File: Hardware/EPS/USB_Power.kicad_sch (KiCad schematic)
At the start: 5 parts

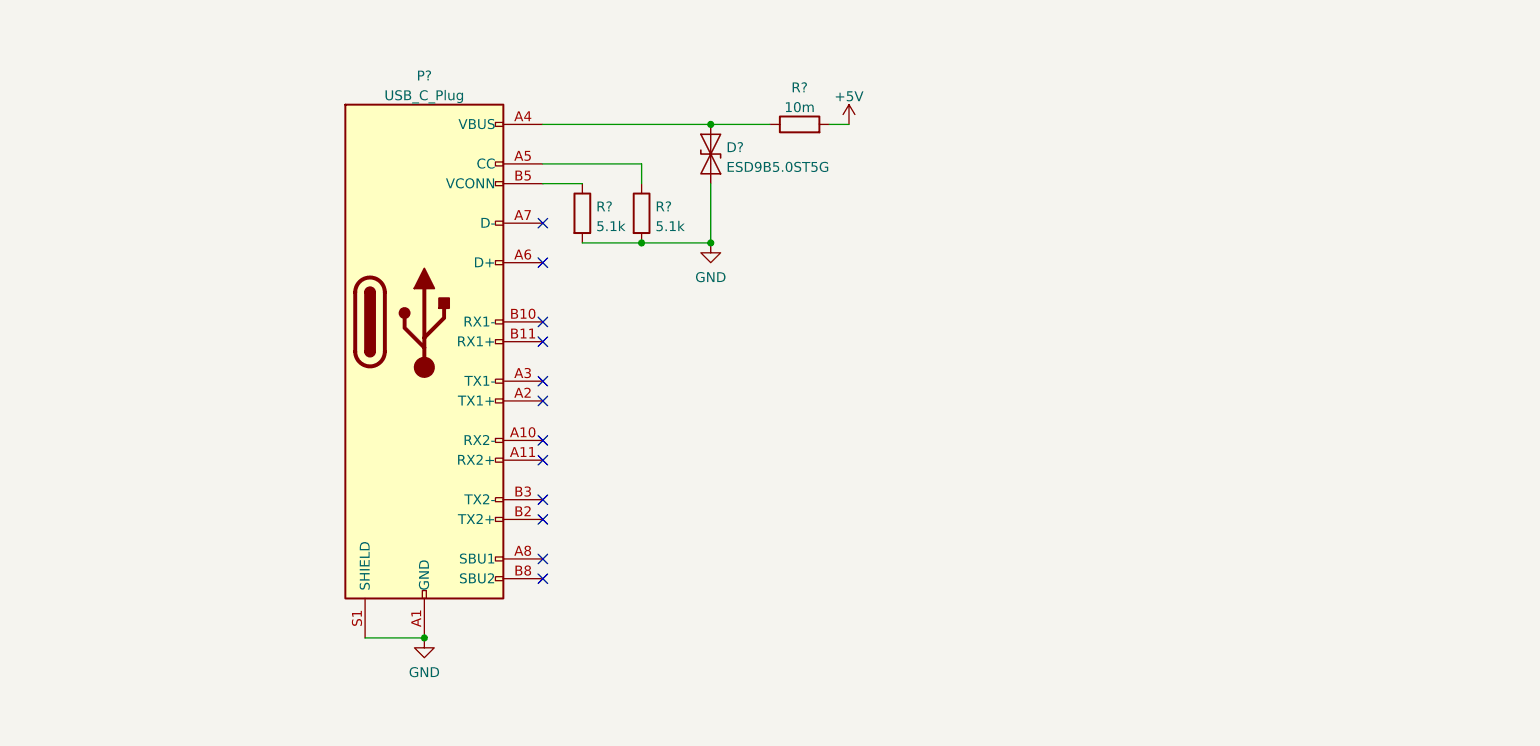
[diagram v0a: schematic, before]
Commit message: Added Power sheet and ESD Protection
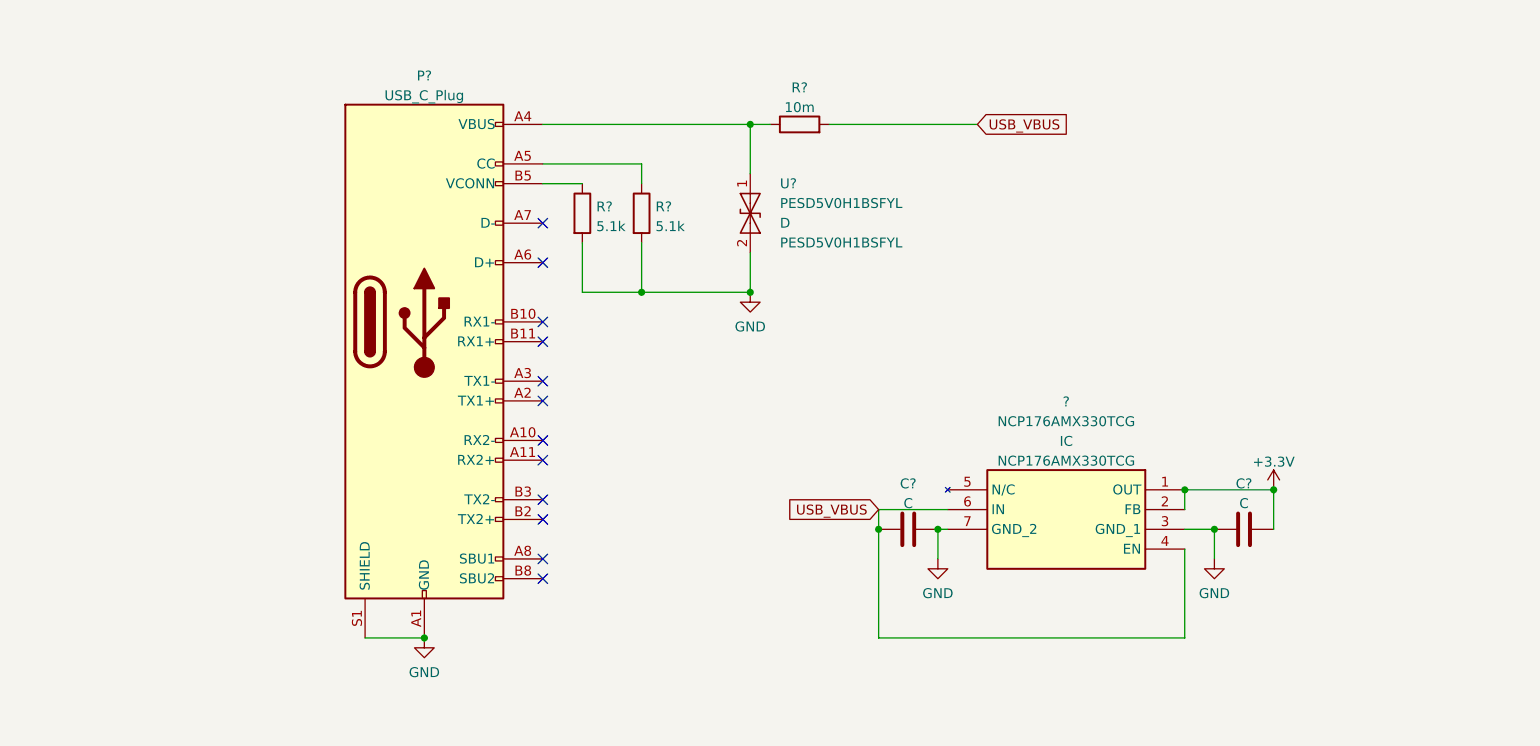
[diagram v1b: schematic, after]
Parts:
- removed D?: ESD9B5.0ST5G, Diode_SMD:D_SOD-923, symbol Diode:ESD9B5.0ST5G
- added ?: NCP176AMX330TCG, symbol NCP176AMX330TCG:NCP176AMX330TCG
- added C? (x2): C, symbol Device:C
- added U?: PESD5V0H1BSFYL, symbol PESD5V0H1BSFYL:PESD5V0H1BSFYL
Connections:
- net GND: now also ?.3 (GND_1), ?.7 (GND_2), C?.1, C?.2, U?.2 (A2)
- net at P?.A4 (VBUS), P?.A9 (VBUS), P?.B4 (VBUS)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: now also U?.1 (A1)
- net +5V renamed USB_VBUS
- net USB_VBUS: now also ?.4 (EN), ?.6 (IN), C?.2
- new net +3.3V: ?.1 (OUT), ?.2 (FB), C?.1

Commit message: EPS v0.0.1
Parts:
- removed R?: 10m, symbol Device:R
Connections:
- net USB_VBUS: now also P?.A4 (VBUS), P?.A9 (VBUS), P?.B4 (VBUS), P?.B9 (VBUS), U?.1 (A1)
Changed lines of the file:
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@@
     (stroke (width 0) (type default) (color 0 0 0 0))
   )
-  (wire (pts (xy 158.75 60.96) (xy 177.8 60.96))
-    (stroke (width 0) (type default) (color 0 0 0 0))
-  )
-  (wire (pts (xy 148.59 60.96) (xy 151.13 60.96))
+  (wire (pts (xy 148.59 60.96) (xy 165.1 60.96))
     (stroke (width 0) (type default) (color 0 0 0 0))
   )
@@
     (stroke (width 0) (type default) (color 0 0 0 0))
   )
-  (global_label "USB_VBUS" (shape input) (at 165.1 110.49 180) (fields_autoplaced)
-    (effects (font (size 1.27 1.27)) (justify right))
-    (property "Intersheet References" "${INTERSHEET_REFS}" (id 0) (at 153.0107 110.4106 0)
-      (effects (font (size 1.27 1.27)) (justify right) hide)
-    )
+  (label "USB_VBUS" (at 165.1 110.49 180)
+    (effects (font (size 1.27 1.27)) (justify right bottom))
   )
-  (global_label "USB_VBUS" (shape input) (at 177.8 60.96 0) (fields_autoplaced)
+  (label "USB_VBUS" (at 153.67 60.96 0)
+    (effects (font (size 1.27 1.27)) (justify left bottom))
+  )
+  (hierarchical_label "USB_VBUS" (shape output) (at 165.1 60.96 0)
     (effects (font (size 1.27 1.27)) (justify left))
-    (property "Intersheet References" "${INTERSHEET_REFS}" (id 0) (at 189.8893 60.8806 0)
-      (effects (font (size 1.27 1.27)) (justify left) hide)
-    )
   )
   (symbol (lib_id "Device:R") (at 127 72.39 0) (unit 1)
@@
     (pin "1")
   )
-  (symbol (lib_id "Device:R") (at 154.94 60.96 90) (unit 1)
-    (in_bom yes) (on_board yes) (fields_autoplaced)
-    (property "Reference" "R?" (id 0) (at 154.94 56.2442 90))
-    (property "Value" "10m" (id 1) (at 154.94 58.7811 90))
-    (property "Footprint" "" (id 2) (at 154.94 62.738 90)
-      (effects (font (size 1.27 1.27)) hide)
-    )
-    (property "Datasheet" "~" (id 3) (at 154.94 60.96 0)
-      (effects (font (size 1.27 1.27)) hide)
-    )
-    (pin "1")
-    (pin "2")
-  )
   (symbol (lib_id "PESD5V0H1BSFYL:PESD5V0H1BSFYL") (at 148.59 72.39 270) (unit 1)

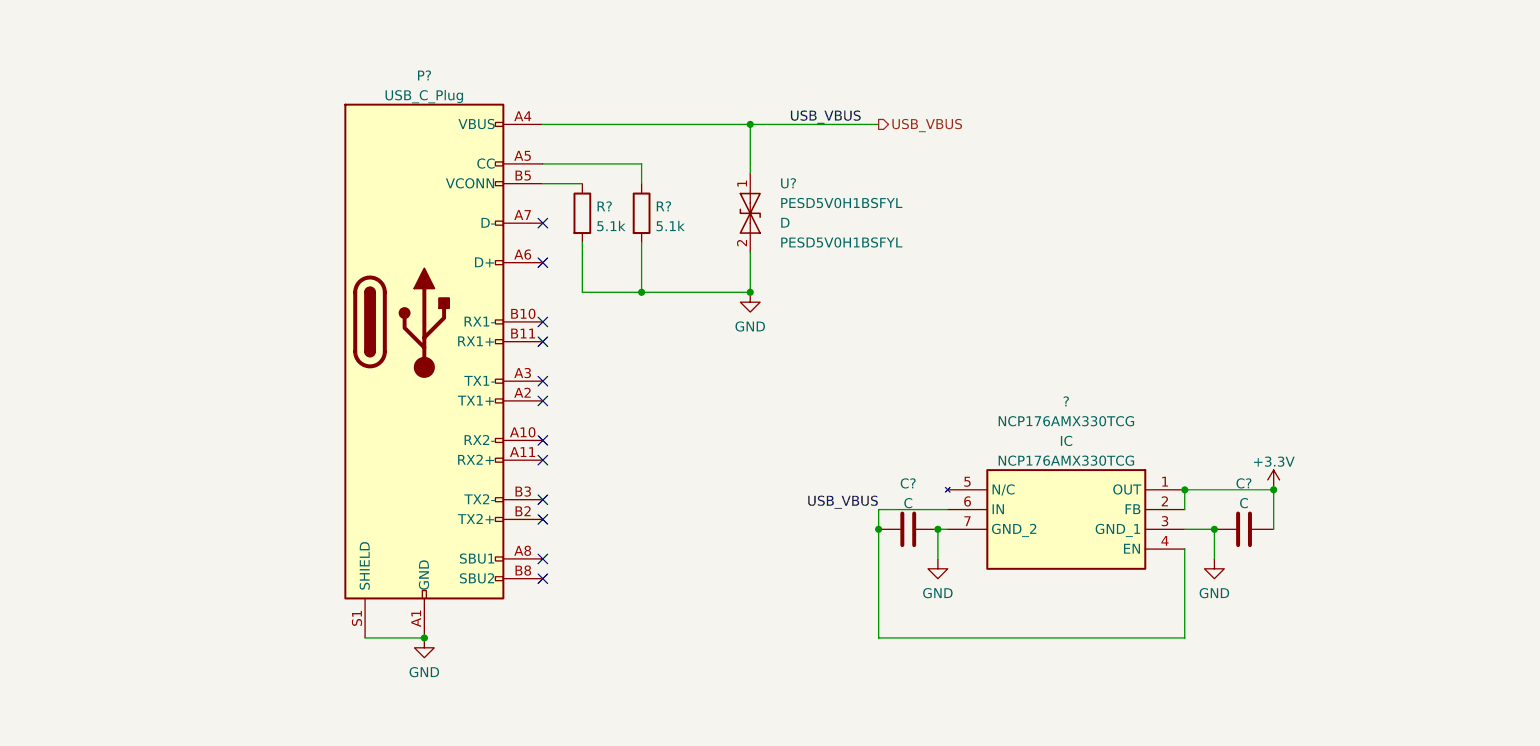
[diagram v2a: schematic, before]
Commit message: Fuse, Power Switch to 3.3V, connector ESD Prot.
v0.0.2
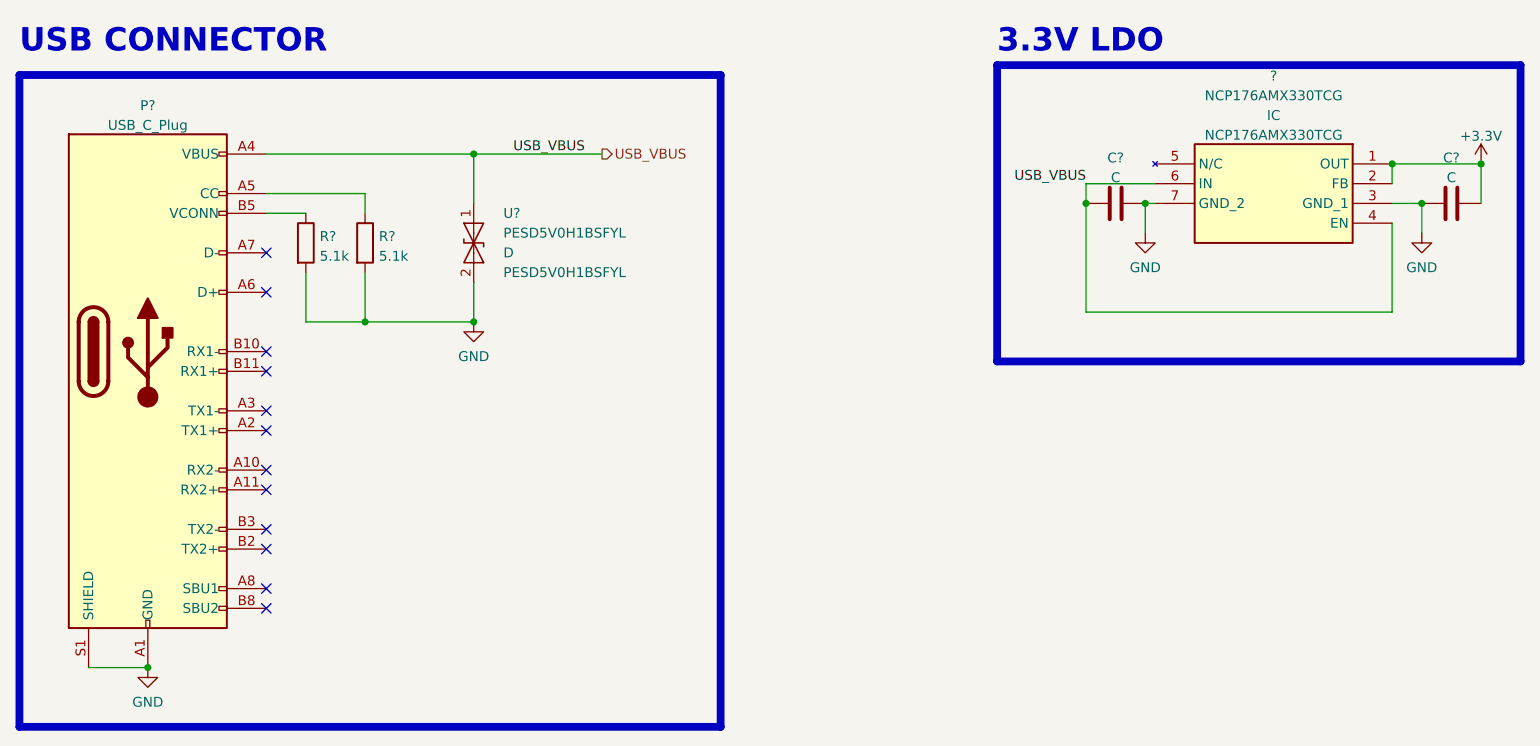
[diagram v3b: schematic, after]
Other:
- note added: "3.3V LDO"
- note added: "USB CONNECTOR"
- title: (none) -> EPS Schematics
- moved on the sheet: ?, C?, P?, R?, U?
